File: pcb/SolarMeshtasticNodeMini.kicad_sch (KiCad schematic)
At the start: 33 parts, among them J2 Conn_01x02_Socket, J3 Conn_01x04_Socket, J4 Conn_01x02_Pin, J5 Conn_01x04_Socket, SW1 SSSS811101, SW2 SW_Push, U1 BQ25185, U2 HT-CT62, U3 HE9073A30MR, U4 APX803L05-32SA-7, U5 TPS22917DBV, U9 SS26_C5350986

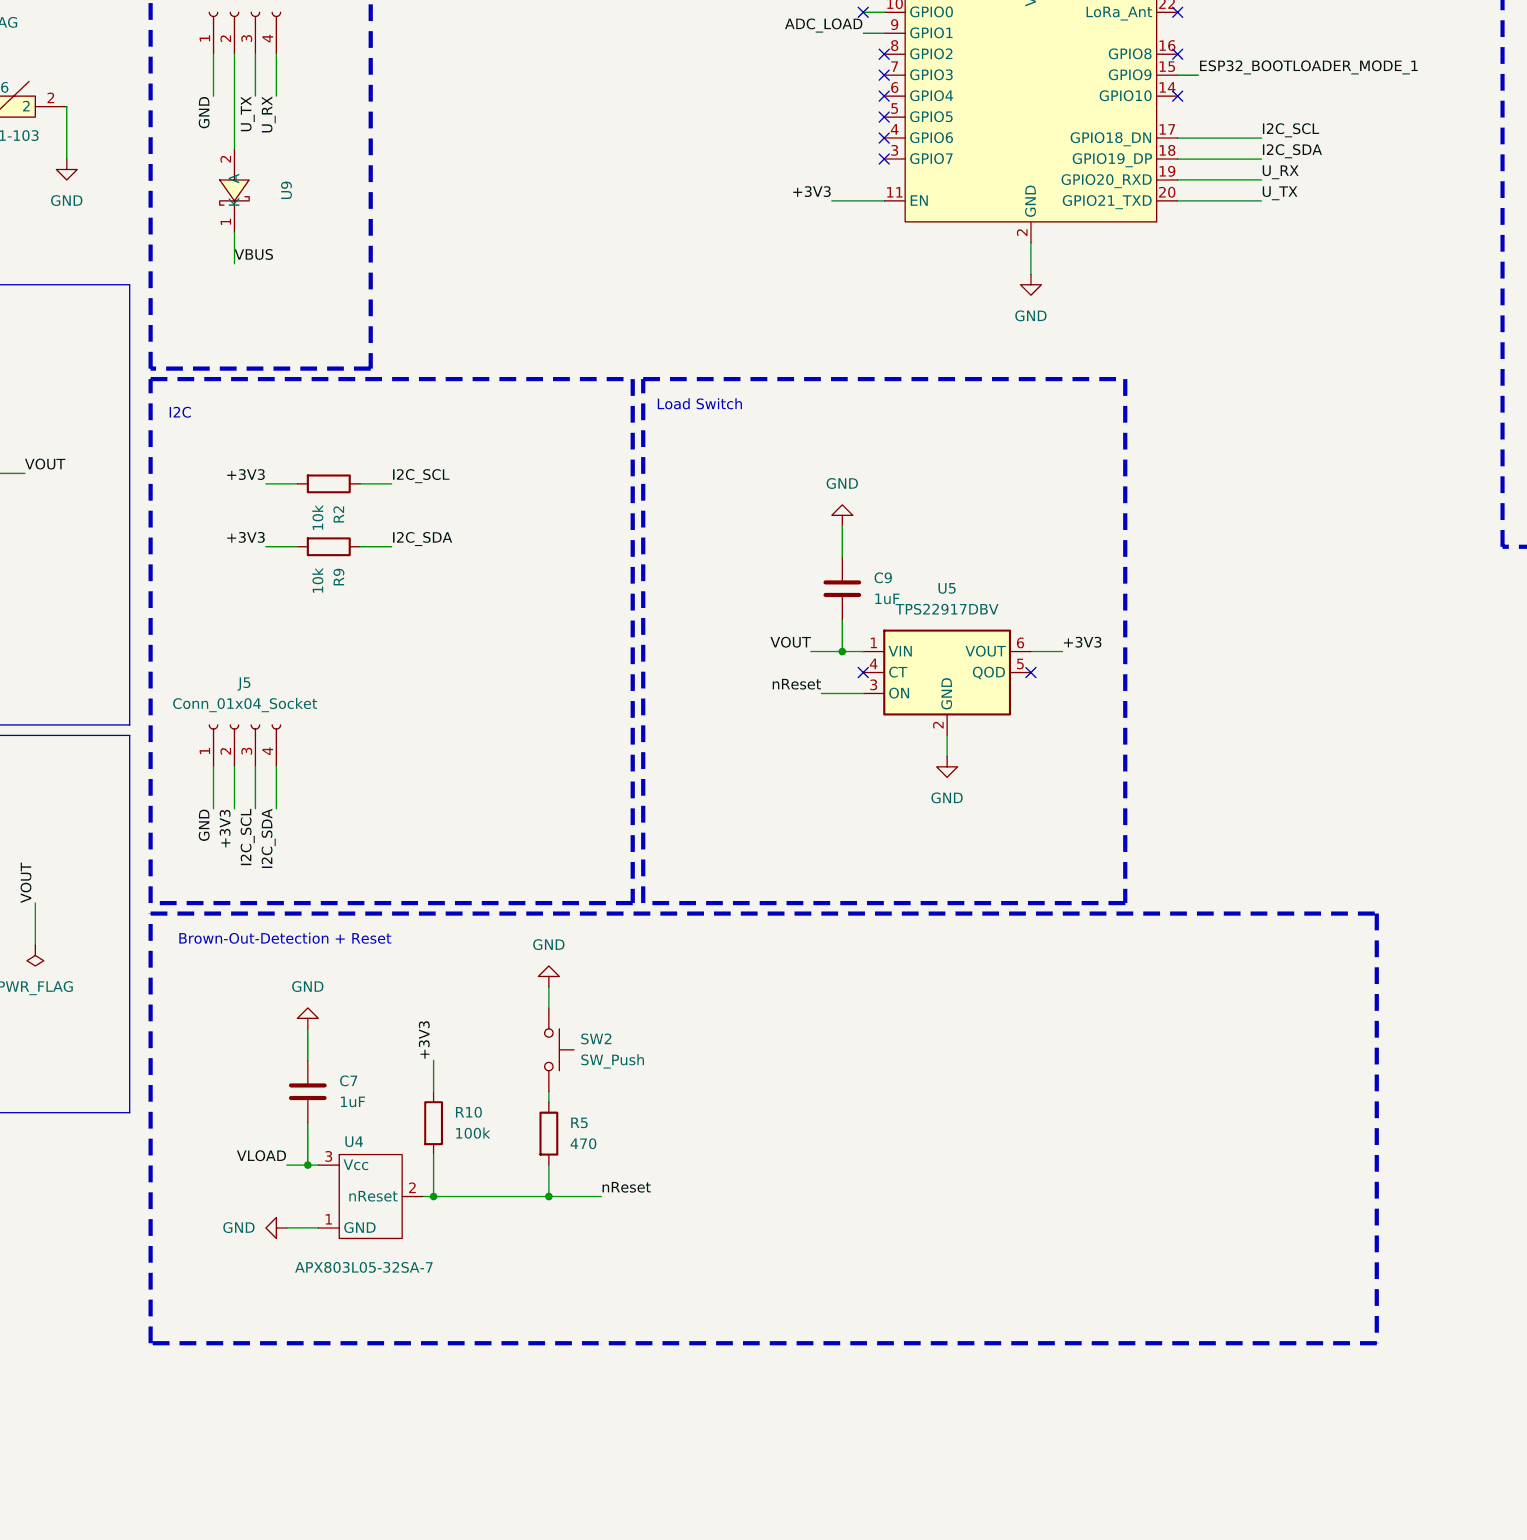
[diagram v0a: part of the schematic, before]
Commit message: pcb, sch: replace reset ic with TI TPS3890 to get rid of bouncing behaviour
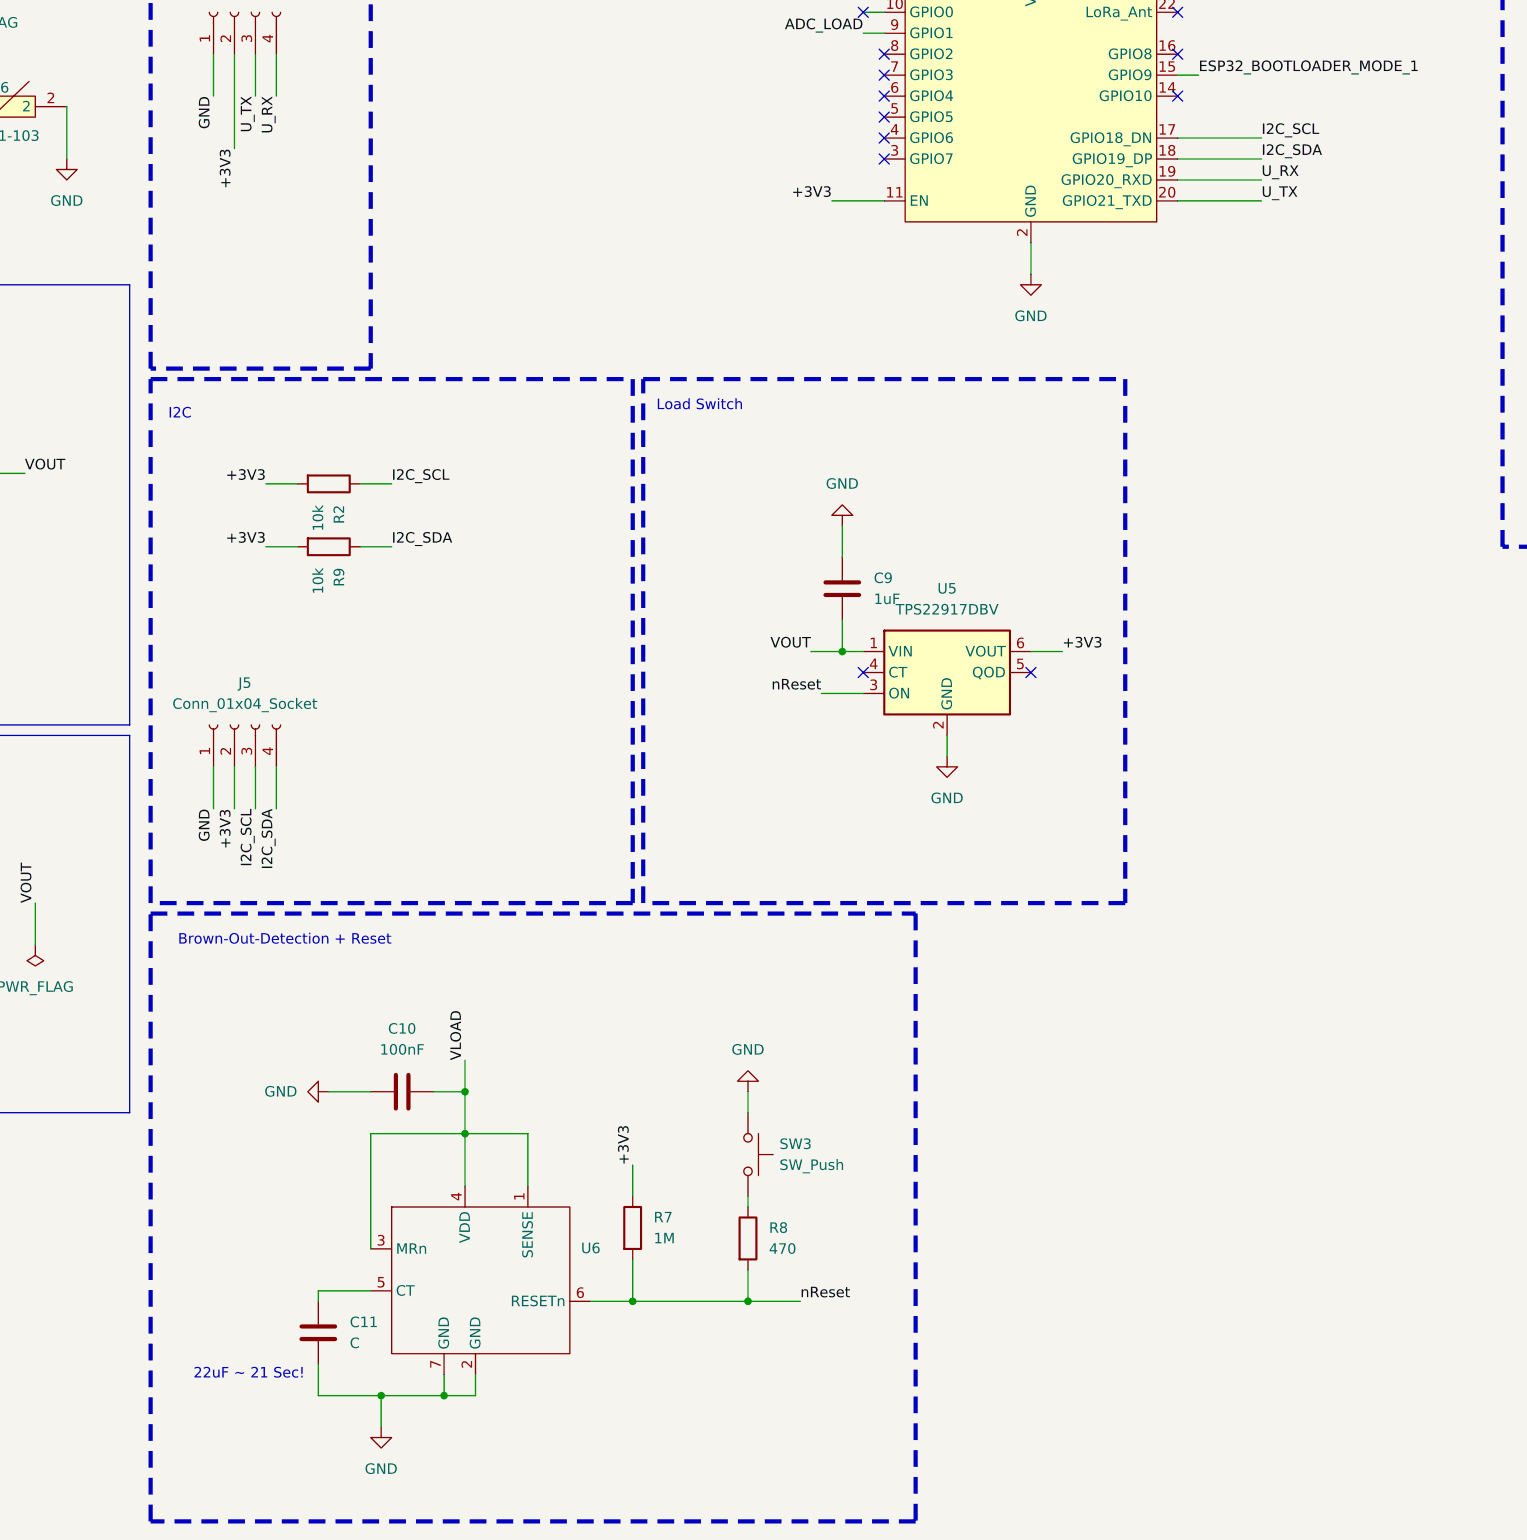
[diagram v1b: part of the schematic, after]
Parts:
- removed C7: 1uF, Capacitor_SMD:C_1206_3216Metric_Pad1.33x1.80mm_HandSolder, symbol Device:C
- removed R10: 100k, Resistor_SMD:R_0805_2012Metric_Pad1.20x1.40mm_HandSolder, symbol Device:R
- removed R5: 470, Resistor_SMD:R_0805_2012Metric_Pad1.20x1.40mm_HandSolder, symbol Device:R
- removed SW2: SW_Push, footprints:SMA_L4.3-W2.6-LS5.1-RD, symbol Switch:SW_Push
- removed U4: APX803L05-32SA-7, footprints:SOT23-3, symbol own_symbols:APX803L05-32SA-7
- removed U9: SS26_C5350986, footprints:SMA_L4.3-W2.6-LS5.1-RD, symbol own_symbols:SS26_C5350986
- added C10: 100nF, Capacitor_SMD:C_0805_2012Metric_Pad1.18x1.45mm_HandSolder, symbol Device:C
- added C11: C, Capacitor_SMD:C_0805_2012Metric_Pad1.18x1.45mm_HandSolder, symbol Device:C
- added R7: 1M, Resistor_SMD:R_0805_2012Metric_Pad1.20x1.40mm_HandSolder, symbol Device:R
- added R8: 470, Resistor_SMD:R_0805_2012Metric_Pad1.20x1.40mm_HandSolder, symbol Device:R
- added SW3: SW_Push, footprints:SMA_L4.3-W2.6-LS5.1-RD, symbol Switch:SW_Push
- added U6: ~, Package_SON:WSON-6-1EP_2x2mm_P0.65mm_EP1x1.6mm, symbol own_symbols:TI_TPS389033DSER
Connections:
- net +3V3: now also J3.2 (Pin_2), R7.1
- net GND: now also C10.1, C11.1, SW3.1, U6.2 (GND), U6.7 (GND)
- net VLOAD: now also C10.2, U6.1 (SENSE), U6.3 (MRn), U6.4 (VDD)
- net nReset: now also R7.2, R8.2, U6.6 (RESETn)
- new net: C11.2, U6.5 (CT)
- new net: R8.1, SW3.2
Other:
- note added: "22uF ~ 21 Sec!"
